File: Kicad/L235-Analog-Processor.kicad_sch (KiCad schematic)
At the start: 224 parts, among them IC1 CA3046Z, J1 Input A, J10 Half Wave In B, J11 Inverted Out B, J12 Invert IN B, J13 Invert IN A, J14 Half Wave In A, J15 Inverted Out A, J16 Full-Wave Rectifier A, J17 Half-Wave Rectifier A, J18 √(A²+B²), J19 A * B / 10, J2 Input B, J20 Root Input |A|, J21 Root Input |A|, J3 Function IN, J4 10A / |B|, J5 Output F(x), J6 Power, J7 Full-Wave Rectifier B, J8 A - B, J9 Half-Wave Rectifier B, Q1 NPN, SW1 71BF30-02-2-06N-circular, SW2 INVERT SWITCH, SW3 71BF30-02-2-06N-circular, SW4 FULL/HALF WAVE, SW6 ADD/SUBTRACT, SW7 POS/NEG HALF WAVE, SW8 INVERT SWITCH, U1 TL082, U10 TL082, U11 TL082, U12 TL082, U13 TL084, U14 CA3046Z, U15 TL082, U16 AD534JH, U16 TL082, U2 TL082, U3 TL082, U4 TL082, U5 TL082, U6 TL082, U7 TL082, U8 TL082, U9 TL082

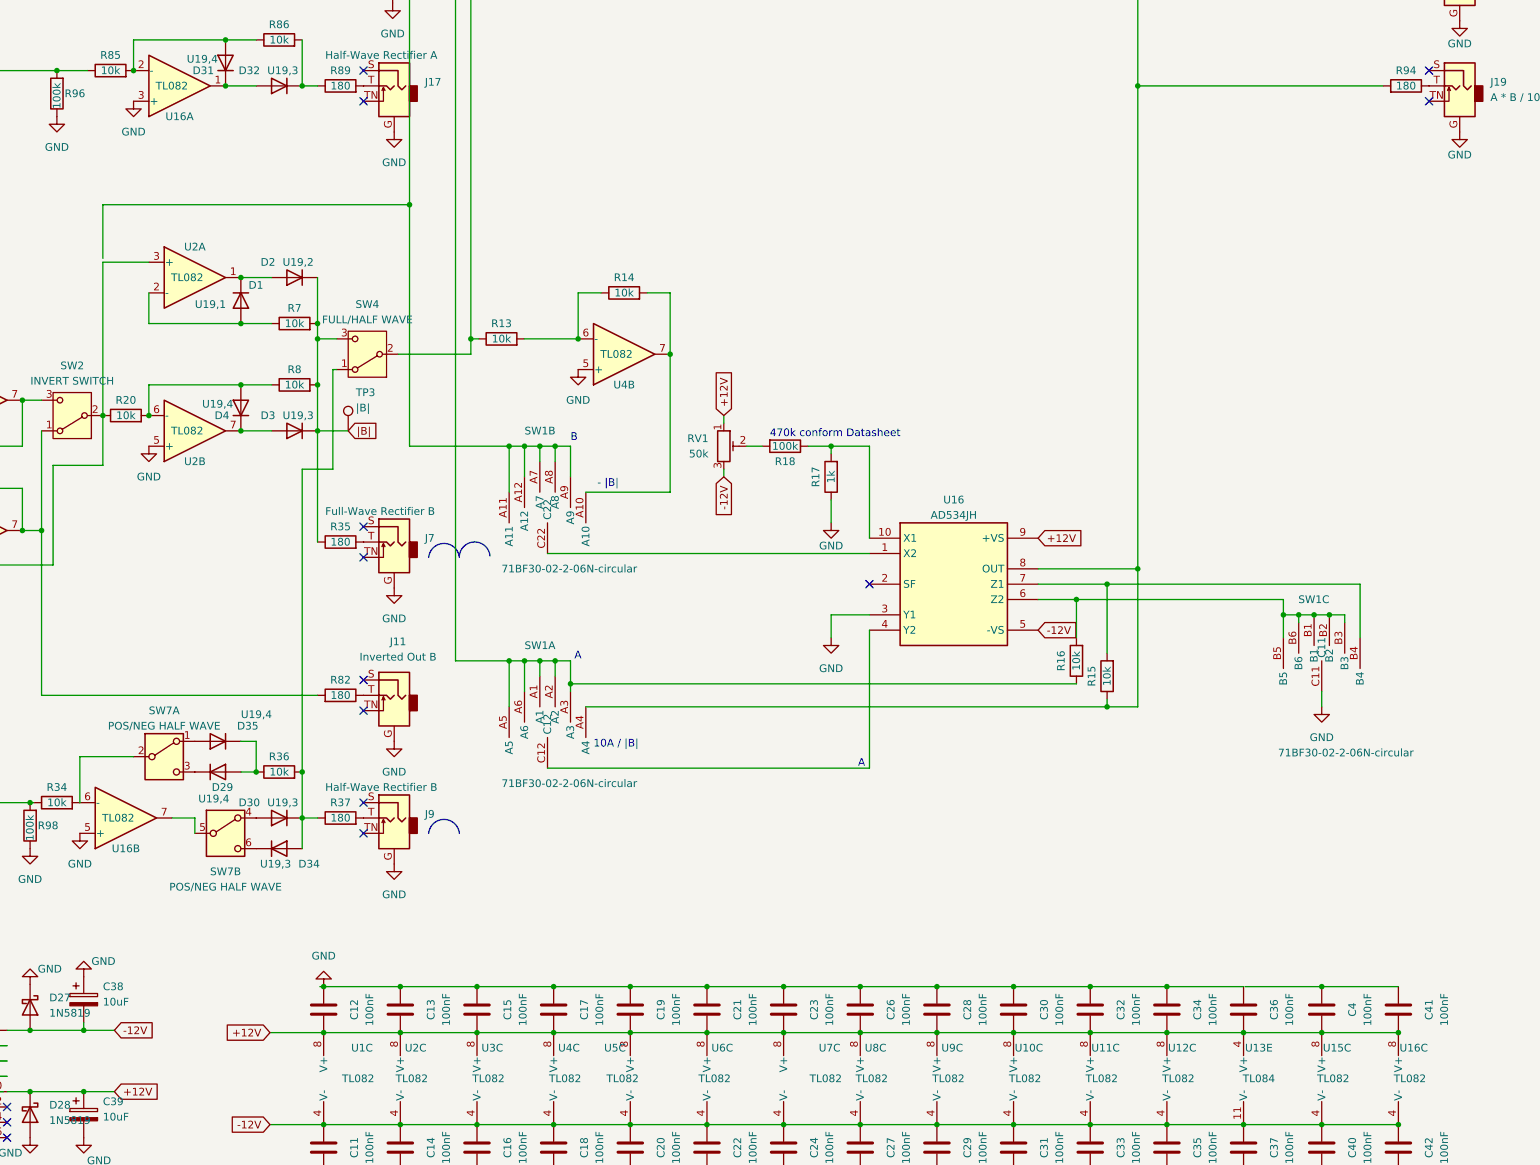
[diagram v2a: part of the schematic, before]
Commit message: fixed double U16 annotation
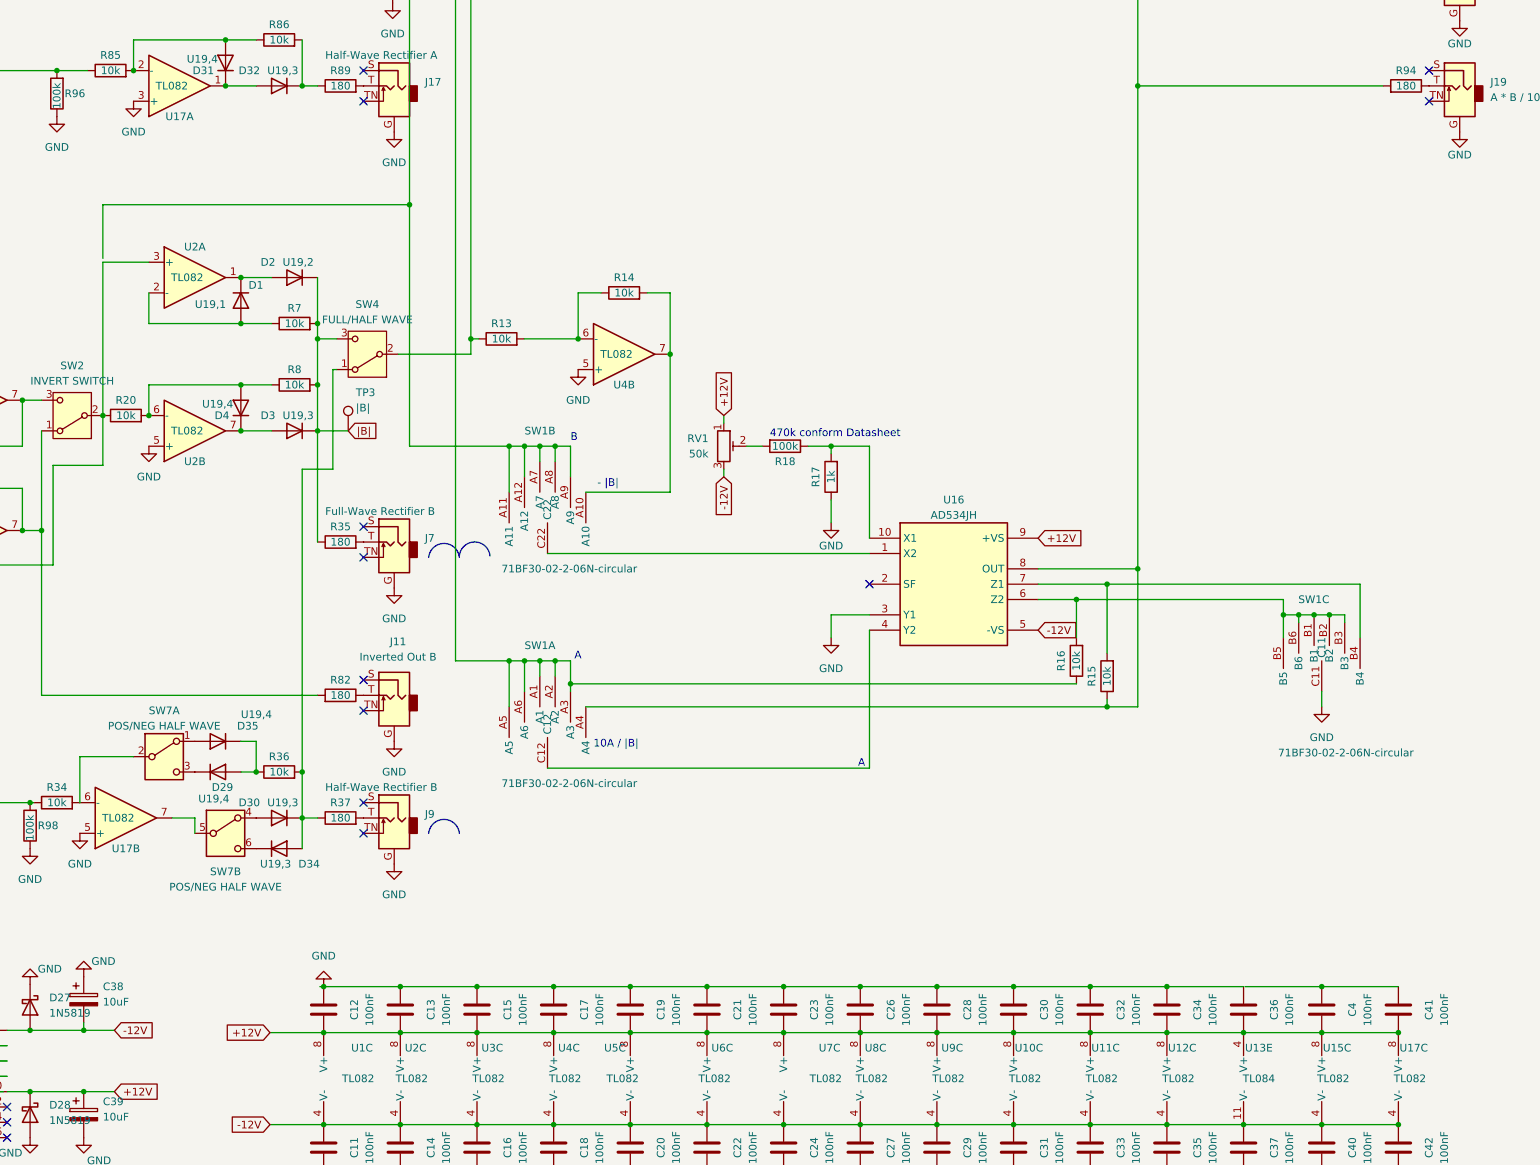
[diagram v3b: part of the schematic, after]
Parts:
- renumbered U16 to U17
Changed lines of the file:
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@@
   (symbol (lib_id "Amplifier_Operational:TL082") (at 287.02 365.76 0) (unit 3)
     (in_bom yes) (on_board yes) (dnp no)
-    (property "Reference" "U16" (at 287.02 360.68 0)
+    (property "Reference" "U17" (at 287.02 360.68 0)
       (effects (font (size 1.27 1.27)))
     )
@@
       (project "L235-Analog-Processor"
         (path "/11565f7a-671a-4a91-8d3b-c6d6401f938b"
-          (reference "U16") (unit 3)
+          (reference "U17") (unit 3)
         )
       )
@@
   (symbol (lib_id "Amplifier_Operational:TL082") (at 73.66 322.58 0) (mirror x) (unit 2)
     (in_bom yes) (on_board yes) (dnp no)
-    (property "Reference" "U16" (at 73.66 327.66 0)
+    (property "Reference" "U17" (at 73.66 327.66 0)
       (effects (font (size 1.27 1.27)))
     )
@@
       (project "L235-Analog-Processor"
         (path "/11565f7a-671a-4a91-8d3b-c6d6401f938b"
-          (reference "U16") (unit 2)
+          (reference "U17") (unit 2)
         )
       )
@@
   (symbol (lib_id "Amplifier_Operational:TL082") (at 82.55 201.295 0) (mirror x) (unit 1)
     (in_bom yes) (on_board yes) (dnp no)
-    (property "Reference" "U16" (at 82.55 206.375 0)
+    (property "Reference" "U17" (at 82.55 206.375 0)
       (effects (font (size 1.27 1.27)))
     )
@@
       (project "L235-Analog-Processor"
         (path "/11565f7a-671a-4a91-8d3b-c6d6401f938b"
-          (reference "U16") (unit 1)
+          (reference "U17") (unit 1)
         )
       )

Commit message: Changed parts to smd and added CV selector
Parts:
- removed D34: U19,3, Diode_THT:D_DO-34_SOD68_P7.62mm_Horizontal, symbol Device:D
- removed D35: U19,4, Diode_THT:D_DO-34_SOD68_P7.62mm_Horizontal, symbol Device:D
- removed IC1, U14: CA3046Z, Package_DIP:DIP-14_W7.62mm_Socket, symbol CA3046Z:CA3046Z
- removed J14: Half Wave In A, Connector_Audio:Jack_3.5mm_PJ311_Horizontal, symbol Connector_Audio:AudioJack2_Ground_SwitchT
- removed J19: A * B / 10, Connector_Audio:Jack_3.5mm_PJ311_Horizontal, symbol Connector_Audio:AudioJack2_Ground_SwitchT
- removed J20, J21: Root Input |A|, Connector_Audio:Jack_3.5mm_PJ311_Horizontal, symbol Connector_Audio:AudioJack2_Ground_SwitchT
- removed Q1: NPN, Resistor_THT:R_Axial_DIN0614_L14.3mm_D5.7mm_P15.24mm_Horizontal, symbol Simulation_SPICE:NPN
- removed R55: 100k, Resistor_THT:R_Axial_DIN0614_L14.3mm_D5.7mm_P15.24mm_Horizontal, symbol Device:R
- removed R56: 1k, Resistor_THT:R_Axial_DIN0614_L14.3mm_D5.7mm_P15.24mm_Horizontal, symbol Device:R
- removed SW1, SW3: 71BF30-02-2-06N-circular, 71BF30-02-2-06N:71BF3002206N, symbol 71BF30-02-2-06N:71BF30-02-2-06N-circular
- removed SW2, SW8: INVERT SWITCH, symbol Switch:SW_SPDT
- removed SW4: FULL/HALF WAVE, symbol Switch:SW_SPDT
- removed SW6: ADD/SUBTRACT, symbol Switch:SW_DPDT_x2
- removed SW7: POS/NEG HALF WAVE, symbol Switch:SW_DPDT_x2
- removed TP3: |B|, TestPoint:TestPoint_THTPad_2.0x2.0mm_Drill1.0mm, symbol Connector:TestPoint
- removed U16: AD534JH, Package_TO_SOT_THT:TO-100-10, symbol AD534LDZ:AD534LDZ
- added C43, C44, C45, C46, C47, C48, C49, C50, C51, C52, C53, C54, C55, C56, C57, C58, C59, C60, C62, C63, C64, C65, C66, C67, C68, C69, C70, C71, C72, C73, C74, C75, C76, C77, C78, C79, C80, C81, C82: 100nF, Capacitor_SMD:C_0402_1005Metric, symbol Device:C
- added C61: 330nF, Capacitor_SMD:C_0402_1005Metric, symbol Device:C
- added IC2: AD633ARZ-RL, Package_SO:SOIC-8_3.9x4.9mm_P1.27mm, symbol AD633ARZ-RL:AD633ARZ-RL
- added R101: 18k, Resistor_SMD:R_0402_1005Metric, symbol Device:R
- added R102, R103, R111, R66: 10k, Resistor_SMD:R_0402_1005Metric, symbol Device:R
- added R104: 4.7k, Resistor_SMD:R_0402_1005Metric, symbol Device:R
- added R105, R106, R107, R108, R109, R113, R60, R61, R62, R90: 1k, Resistor_SMD:R_0402_1005Metric, symbol Device:R
- added R110, R65: 2k, Resistor_SMD:R_0402_1005Metric, symbol Device:R
- added R112: 100k, Resistor_SMD:R_0402_1005Metric, symbol Device:R
- added R63: 4.3k, Resistor_SMD:R_0402_1005Metric, symbol Device:R
- added R64: 3k, Resistor_SMD:R_0402_1005Metric, symbol Device:R
- added RV10, RV9: 100k, Potentiometer_THT:Potentiometer_Alpha_RD901F-40-00D_Single_Vertical, symbol Device:R_Potentiometer
- added RV11, RV12: 50k, Potentiometer_THT:Potentiometer_Alpha_RD901F-40-00D_Single_Vertical, symbol Device:R_Potentiometer
- added TR1, TR2, TR3, TR4, TR5: FMBM5551, Package_TO_SOT_SMD:SOT-23-6_Handsoldering, symbol Macbeth:BC847CDW1T1G
- added U16: RC4580, Package_SO:SOIC-8_3.9x4.9mm_P1.27mm, symbol Amplifier_Operational:RC4580
- added U18: LM4040DBZ-10, Package_TO_SOT_SMD:SOT-23, symbol Reference_Voltage:LM4040DBZ-10
- added U19, U31: 74HC148, Package_SO:SOIC-16W_5.3x10.2mm_P1.27mm, symbol 74xx:74LS348
- added U20, U21, U29, U30: LM339, Package_SO:SOIC-14_3.9x8.7mm_P1.27mm, symbol Comparator:LM339
- added U22, U23, U24, U25, U26, U27, U28, U32, U33, U34, U35: 74LS151, Package_SO:TSSOP-16-1EP_4.4x5mm_P0.65mm_EP3x3mm, symbol 4xxx:4051
- added U36: LM78M05_TO252, Package_TO_SOT_SMD:TO-252-2, symbol Regulator_Linear:LM78M05_TO252
- C1, C11, C12, C13, C14, C15, C16, C17, C18, C19, C2, C20, C21, C22, C23, C24, C26, C27, C28, C29, C30, C31, C32, C33, C34, C35, C36, C37, C4, C40, C41, C42, C5, C6, C8: footprint Capacitor_THT:C_Rect_L7.0mm_W3.5mm_P2.50mm_P5.00mm -> Capacitor_SMD:C_0402_1005Metric
- C10, C25, C3, C7, C9: footprint Capacitor_THT:C_Rect_L7.0mm_W3.5mm_P2.50mm_P5.00mm -> Capacitor_THT:C_Rect_L7.0mm_W2.5mm_P5.00mm
- C38, C39: footprint Capacitor_THT:C_Disc_D5.0mm_W2.5mm_P5.00mm -> Capacitor_THT:C_Radial_D5.0mm_H7.0mm_P2.00mm
- D1, D10, D11, D12, D13, D14, D15, D16, D17, D18, D19, D2, D20, D21, D22, D23, D24, D25, D26, D29, D3, D30, D31, D32, D4, D5, D6, D7, D8, D9: footprint Diode_THT:D_DO-34_SOD68_P7.62mm_Horizontal -> Diode_SMD:D_0402_1005Metric
- D27, D28: footprint Diode_THT:D_DO-41_SOD81_P10.16mm_Horizontal -> Diode_SMD:D_0402_1005Metric
- J1, J11, J15, J16, J17, J18, J2, J3, J5, J7, J8: footprint Connector_Audio:Jack_3.5mm_PJ311_Horizontal -> Custom_Footprints:Cliff_3.5mm_Stereo_Jack
- J10: value Half Wave In B -> Half Wave A + -B; footprint Connector_Audio:Jack_3.5mm_PJ311_Horizontal -> Custom_Footprints:Cliff_3.5mm_Stereo_Jack
- J12: value Invert IN B -> CV Select; footprint Connector_Audio:Jack_3.5mm_PJ311_Horizontal -> Custom_Footprints:Cliff_3.5mm_Stereo_Jack
- J13: value Invert IN A -> CV Select; footprint Connector_Audio:Jack_3.5mm_PJ311_Horizontal -> Custom_Footprints:Cliff_3.5mm_Stereo_Jack
- J4: value 10A / |B| -> ( 10A / |B| ) / ( A * B / 10 ); footprint Connector_Audio:Jack_3.5mm_PJ311_Horizontal -> Custom_Footprints:Cliff_3.5mm_Stereo_Jack
- J6: footprint Resistor_THT:R_Axial_DIN0614_L14.3mm_D5.7mm_P15.24mm_Horizontal -> Custom_Footprints:Eurorack_16_pin_header
- J9: value Half-Wave Rectifier B -> Negative Half-Wave Rectifier B; footprint Connector_Audio:Jack_3.5mm_PJ311_Horizontal -> Custom_Footprints:Cliff_3.5mm_Stereo_Jack
- R1, R10, R11, R12, R13, R14, R17, R19, R20, R21, R22, R23, R24, R25, R26, R27, R28, R29, R3, R30, R31, R32, R33, R34, R35, R36, R37, R39, R40, R41, R42, R43, R44, R45, R46, R47, R48, R49, R5, R50, R51, R52, R53, R54, R57, R58, R59, R6, R67, R68, R69, R7, R70, R71, R72, R73, R74, R75, R76, R77, R78, R79, R8, R80, R81, R82, R84, R85, R86, R87, R88, R89, R9, R91, R92, R93, R99: footprint Resistor_THT:R_Axial_DIN0614_L14.3mm_D5.7mm_P15.24mm_Horizontal -> Resistor_SMD:R_0402_1005Metric
- R100, R4: value 100k -> 10k; footprint Resistor_THT:R_Axial_DIN0614_L14.3mm_D5.7mm_P15.24mm_Horizontal -> Resistor_SMD:R_0402_1005Metric
- R15: value 10k -> 100k; footprint Resistor_THT:R_Axial_DIN0614_L14.3mm_D5.7mm_P15.24mm_Horizontal -> Resistor_SMD:R_0402_1005Metric
- R16: value 10k -> 3k; footprint Resistor_THT:R_Axial_DIN0614_L14.3mm_D5.7mm_P15.24mm_Horizontal -> Resistor_SMD:R_0402_1005Metric
- R18: value 100k -> 300k; footprint Resistor_THT:R_Axial_DIN0614_L14.3mm_D5.7mm_P15.24mm_Horizontal -> Resistor_SMD:R_0402_1005Metric
- R2, R95, R96, R97: value 100k -> 1k; footprint Resistor_THT:R_Axial_DIN0614_L14.3mm_D5.7mm_P15.24mm_Horizontal -> Resistor_SMD:R_0402_1005Metric
- R38: value 10k -> 180; footprint Resistor_THT:R_Axial_DIN0614_L14.3mm_D5.7mm_P15.24mm_Horizontal -> Resistor_SMD:R_0402_1005Metric
- R83: value 10k -> 1k; footprint Resistor_THT:R_Axial_DIN0614_L14.3mm_D5.7mm_P15.24mm_Horizontal -> Resistor_SMD:R_0402_1005Metric
- R94: value 180 -> 1k; footprint Resistor_THT:R_Axial_DIN0614_L14.3mm_D5.7mm_P15.24mm_Horizontal -> Resistor_SMD:R_0402_1005Metric
- R98: value 100k -> 3k; footprint Resistor_THT:R_Axial_DIN0614_L14.3mm_D5.7mm_P15.24mm_Horizontal -> Resistor_SMD:R_0402_1005Metric
- RV1, RV2, RV3, RV4, RV5, RV6: footprint Resistor_THT:R_Axial_DIN0614_L14.3mm_D5.7mm_P15.24mm_Horizontal -> Potentiometer_THT:Potentiometer_Bourns_3339H_Vertical
- RV7: footprint (none) -> Potentiometer_THT:Potentiometer_Alps_RK163_Single_Horizontal
- RV8: footprint Resistor_THT:R_Axial_DIN0614_L14.3mm_D5.7mm_P15.24mm_Horizontal -> Potentiometer_THT:Potentiometer_Alps_RK163_Single_Horizontal
- U1, U10, U11, U12, U2, U3, U4, U5, U6, U7, U8, U9: footprint Package_DIP:DIP-8_W7.62mm_Socket -> Package_SO:SOIC-8_3.9x4.9mm_P1.27mm
- U13: footprint Package_DIP:DIP-14_W7.62mm_Socket -> Package_SO:SOIC-14_3.9x8.7mm_P1.27mm
- U15, U17: footprint Package_DIP:DIP-8_W7.62mm_Socket -> Package_SO:SO-8_3.9x4.9mm_P1.27mm
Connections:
- net +12V: now also C4.1, C41.1, U15.8 (V+), U17.8 (V+), C45.1, C47.1, C49.2, C52.2, C60.2, C61.1, C64.2, C66.2, C67.2, C68.2, C69.2, C70.2, C71.2, C73.2, C82.2, IC2.6 (+VS), U20.3 (V+), U21.3 (V+), U22.16 (VDD), U23.16 (VDD), U24.16 (VDD), U25.16 (VDD), U26.16 (VDD), U27.16 (VDD), U28.16 (VDD), U32.16 (VDD), U33.16 (VDD), U34.16 (VDD), U35.16 (VDD), U36.1 (VI); no longer C11.1, C11.2, C12.2, C13.2, C14.1, C14.2, C15.2, C16.1, C16.2, C17.2, C18.1, C18.2, C19.2, C20.1, C20.2, C21.2, C22.1, C22.2, C23.2, C24.1, C24.2, C26.2, C27.1, C27.2, C28.2, C29.1, C29.2, C3.2, C30.2, C31.1, C31.2, C32.2, C33.1, C33.2, C34.2, C35.1, C35.2, C36.2, C37.1, C37.2, C38.1, C38.2, C39.2, C9.2, D10.1 (K), D26.1 (K), D27.1 (K), D27.2 (A), D28.2 (A), D9.1 (K), J1.G, J10.G, J11.G, J12.G, J13.G, J15.G, J16.G, J17.G, J18.G, J2.G, J3.G, J4.G, J5.G, J6.1 (Pin_1), J6.2 (Pin_2), J6.3 (Pin_3), J6.4 (Pin_4), J6.5 (Pin_5), J6.6 (Pin_6), J6.7 (Pin_7), J6.8 (Pin_8), J7.G, J8.G, J9.G, R10.1, R100.1, R17.1, R25.2, R26.1, R31.1, R4.1, R48.2, R59.1, R71.2, R72.1, R75.1, R76.2, R78.2, R79.2, R80.1, R95.1, R96.1, R97.1, R98.1, R99.1, RV1.3, U1.4 (V-), U10.4 (V-), U10.5 (+), U11.3 (+), U11.4 (V-), U11.5 (+), U12.3 (+), U12.4 (V-), U12.5 (+), U13.10 (+), U13.11 (V-), U13.13 (-), U15.3 (+), U15.5 (+), U17.3 (+), U17.5 (+), U2.4 (V-), U2.5 (+), U3.4 (V-), U3.5 (+), U4.4 (V-), U4.5 (+), U5.3 (+), U5.4 (V-), U6.2 (-), U6.4 (V-), U7.3 (+), U7.4 (V-), U8.4 (V-), U8.5 (+), U9.3 (+), U9.4 (V-)
- net <X>: now also R112.1, R113.1, U34.15 (X2)
- net X: now also U22.3 (X)
- net |A|: now also D5.1 (K), D8.1 (K), R21.1, R5.2, R6.2, R88.1
- net |B|: now also R13.1, RV3.2, RV3.3
- net √|x| or X²: now reaches R54.1, U10.7
- net √|x| or X²: now also U34.12 (X3), U34.14 (X1)
- net (-dX/dt) or (-dX/dt*1/100): now reaches R57.1, R58.2, U7.1
- net (-dX/dt) or (-dX/dt*1/100): now also U34.1 (X4), U34.5 (X5)
- net ln |x|: now reaches RV5.2, RV5.3, U11.7
- net ln |x|: now also U34.13 (X0)
- net Function Out: now reaches D12.2 (A), D17.1 (K), RV8.1
- net Function Out: now also U34.3 (X)
- net at C5.1, R43.2, U9.2 (-): now also TR3.6
- net at C1.1, RV2.3, U5.2 (-): now also TR5.6
- net at R99.2: now also R98.1, R62.2, U20.5 (+); no longer R21.1
- net B: now reaches R20.1, U2.3 (+)
- net B: now also R100.1, R11.1, R34.1, R4.1, U1.6 (-), U1.7, U23.1 (X4), U23.12 (X3), U23.13 (X0), U23.14 (X1), U23.15 (X2); no longer J10.TN
- net at R94.1: now also R95.2, U21.5 (+)
- net at C2.2, R33.1, R33.2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: now also TR2.4
- net GND: now reaches C4.2, C41.2
- net GND: now also C11.1, C12.2, C13.2, C14.1, C15.2, C16.1, C17.2, C18.1, C19.2, C20.1, C21.2, C22.1, C23.2, C24.1, C26.2, C27.1, C28.2, C29.1, C3.2, C30.2, C31.1, C32.2, C33.1, C34.2, C35.1, C36.2, C37.1, C38.1, C39.2, C40.1, C42.1, C9.2, D10.1 (K), D26.1 (K), D27.1 (K), D28.2 (A), D9.1 (K), J1.G, J10.G, J11.G, J12.G, J13.G, J15.G, J16.G, J17.G, J18.G, J2.G, J3.G, J4.G, J5.G, J6.3 (Pin_3), J6.4 (Pin_4), J6.5 (Pin_5), J6.6 (Pin_6), J6.7 (Pin_7), J6.8 (Pin_8), J7.G, J8.G, J9.G, R10.1, R15.1, R17.1, R25.2, R31.1, R48.2, R59.1, R72.1, R75.1, R78.2, R79.2, R80.1, R97.1, R99.1, U10.5 (+), U11.3 (+), U11.5 (+), U12.3 (+), U12.5 (+), U13.10 (+), U13.13 (-), U15.3 (+), U15.5 (+), U17.3 (+), U17.5 (+), U2.5 (+), U3.5 (+), U4.5 (+), U5.3 (+), U6.2 (-), U7.3 (+), U8.5 (+), U9.3 (+), C43.1, C44.1, C45.2, C46.1, C47.2, C48.1, C49.1, C50.1, C51.1, C52.1, C53.1, C54.1, C55.1, C56.1, C57.1, C58.1, C59.1, C60.1, C61.2, C62.1, C63.1, C64.1, C65.1, C66.1, C67.1, C68.1, C69.1, C70.1, C71.1, C72.1, C73.1, C74.2, C75.1, C76.2, C77.1, C78.1, C80.2, C81.1, C82.1, R101.2, R109.1, R111.1, R64.1, R66.1, RV10.3, RV11.3, RV12.3, RV9.3, TR2.3, TR3.1, TR4.3, TR5.1, U16.5 (+), U18.2 (A), U19.5 (EI), U19.8 (GND), U22.6 (Inh), U22.7 (VEE), U23.6 (Inh), U23.7 (VEE), U24.2 (X6), U24.6 (Inh), U24.7 (VEE), U25.6 (Inh), U25.7 (VEE), U26.5 (X5), U26.6 (Inh), U26.7 (VEE), U27.1 (X4), U27.12 (X3), U27.13 (X0), U27.14 (X1), U27.15 (X2), U27.6 (Inh), U27.7 (VEE), U28.1 (X4), U28.12 (X3), U28.13 (X0), U28.14 (X1), U28.15 (X2), U28.5 (X5), U28.6 (Inh), U28.7 (VEE), U31.5 (EI), U31.8 (GND), U32.6 (Inh), U32.7 (VEE), U33.6 (Inh), U33.7 (VEE), U34.6 (Inh), U34.7 (VEE), U35.6 (Inh), U35.7 (VEE), U36.2 (GND)
- net A: now reaches R19.1, R9.1, U3.3 (+)
- net A: now also R84.1, R85.1, U1.1, U1.2 (-), U15.2 (-), R103.1, U24.1 (X4), U24.12 (X3), U24.13 (X0), U24.14 (X1), U24.15 (X2), U27.2 (X6), U28.2 (X6); no longer R16.1
- net 10V REF: now reaches R16.2
- net 10V REF: now also J1.TN, J2.TN, R2.2, R98.2, C43.2, R110.2, R65.2, U18.1 (K)
- net -12V: now reaches C40.2, C42.2, U15.4 (V-), U17.4 (V-)
- net -12V: now also C11.2, C14.2, C16.2, C18.2, C20.2, C22.2, C24.2, C27.2, C29.2, C31.2, C33.2, C35.2, C37.2, C38.2, D27.2 (A), J6.1 (Pin_1), J6.2 (Pin_2), R26.1, R71.2, R76.2, RV1.3, U1.4 (V-), U10.4 (V-), U11.4 (V-), U12.4 (V-), U13.11 (V-), U2.4 (V-), U3.4 (V-), U4.4 (V-), U5.4 (V-), U6.4 (V-), U7.4 (V-), U8.4 (V-), U9.4 (V-), C44.2, C46.2, C50.2, C51.2, C53.2, C54.2, C55.2, C57.2, C58.2, C59.2, C63.2, C65.2, C72.2, C75.2, C77.2, C78.2, C81.2, IC2.3 (-VS), U16.4 (V-), U20.12 (V-), U21.12 (V-), U22.8 (VSS), U23.8 (VSS), U24.8 (VSS), U25.8 (VSS), U26.8 (VSS), U27.8 (VSS), U28.8 (VSS), U29.12 (V-), U30.12 (V-), U32.8 (VSS), U33.8 (VSS), U34.8 (VSS), U35.8 (VSS)
- net at R96.2: now also R95.1, U21.11 (+); no longer R85.1
- net at R45.1, U9.5 (+): now also TR3.3, TR3.4
- net X²: now reaches D26.2 (A), R46.1, R49.2, U9.7
- net X²: now also U35.1 (X4), U35.12 (X3), U35.5 (X5)
- net B|: now reaches D30.1 (K), R36.2, R37.1
- net B|: now also D32.1 (K), R38.1, R86.2, R89.1
- net at D30.2 (A): now also D29.1 (K), U17.7
- net at R36.1: now also D29.2 (A), R34.2, U17.6 (-); no longer D29.1 (K)
- net at R9.2, U4.3 (+): now also R10.2
- net at R12.1, U4.2 (-): now also R11.2
- net √|x|: now reaches R47.2, R48.1
- net √|x|: now also U35.13 (X0), U35.14 (X1), U35.15 (X2)
- net CA3046_B3: now reaches U10.3 (+)
- net CA3046_B3: now also TR4.1, U35.3 (X)
- net F1: now reaches C7.2, R57.2, U7.2 (-)
- net F1: now also U33.12 (X3), U33.13 (X0), U33.14 (X1), U33.15 (X2), U33.5 (X5)
- net -A: now reaches R84.2, R87.2, U15.1
- net F2: now reaches R58.1
- net F2: now also U33.3 (X)
- net -Output: now reaches D13.2 (A), D16.1 (K), R67.1, R68.2, U12.7
- net at R30.1, U13.1, U13.2 (-): now also TR2.5
- net at R22.2, R23.1: now also TR5.5
- net at R29.2, R32.2: now also TR2.2
- net at R44.2: now also TR3.2, TR3.5
- net at C25.1, R27.1, U11.2 (-): now also TR1.4, TR1.6
- net at R24.2, U5.7: now also TR1.1
- net at R28.1, U6.7: now also TR1.3
- net Volt_ref_X: now reaches R17.2, R18.1
- net Volt_ref_X: now also U25.1 (X4), U25.12 (X3), U25.13 (X0), U25.14 (X1), U25.15 (X2), U25.5 (X5)
- net at R15.2: now also R16.1, R60.2, U29.5 (+)
- net at R39.1, U15.6 (-): now also R4.2; no longer R38.2
- net -B: now reaches R39.2, R82.2, U15.7
- net at R54.2, U10.6 (-): now also TR4.4
- net -|B|: now reaches R14.2, U4.7
- net -|B|: now also U23.5 (X5)
- net F1-1/100: now reaches C7.1
- net F1-1/100: now also U32.3 (X)
- net √(A²+B²): now reaches C25.2, R27.2, R93.2, U11.1
- net √(A²+B²): now also U22.14 (X1)
- net at C6.1, R52.1, U10.2 (-): now also TR4.6
- net at R53.2: now also TR4.2, TR4.5
- net A - B: now reaches R12.2, R92.2, U4.1
- net A - B: now also U22.1 (X4)
- new net: C74.1, C76.1, C80.1, U16.8 (V+), U29.3 (V+), U30.3 (V+)
- new net: J13.T, R110.1, R111.2, RV12.1
- new net: R112.2, U32.1 (X4)
- new net: J12.T, R65.1, R66.2, RV11.1
- new net: U29.1, U31.12 (2)
- new net: R60.1, R61.2, U29.7 (+)
- new net: R90.1, R94.2, U20.9 (+)
- new net: J10.T, R38.2
- new net: R102.2, U26.1 (X4), U26.12 (X3), U26.13 (X0), U26.14 (X1), U26.15 (X2)
- new net: R108.1, R109.2, U30.9 (+)
- new net: R107.1, R108.2, U30.11 (+)
- new net: U19.2 (5), U21.2
- new net: IC2.4 (Z), U16.1
- new net: R103.2, U27.5 (X5)
- new net: TR1.2, TR1.5, TR2.1, TR2.6
- new net: U30.14, U31.4 (7)
- new net: R105.2, R61.1, U29.11 (+)
- new net: U29.13, U31.13 (3)
- new net: U29.14, U31.1 (4)
- new net: R105.1, R106.2, U29.9 (+)
- new net: U29.2, U31.11 (1)
- new net: R83.1, R90.2, U20.11 (+)
- new net: U19.11 (1), U20.2
- new net: J2.T, RV10.1
- new net: R62.1, R83.2, U20.7 (+)
- new net: J1.T, RV9.1
- new net: R1.1, RV9.2
- new net: U19.13 (3), U20.13
- new net: U30.2, U31.2 (5)
- new net: U30.13, U31.3 (6)
- new net: R100.2, R101.1, U23.2 (X6)
- new net: U19.1 (4), U20.14
- new net: R104.2, U26.2 (X6)
- new net: U19.4 (7), U21.14
- new net: R96.1, R97.2, U21.9 (+)
- new net: R113.2, U32.5 (X5)
- new net: R106.1, R107.2, U30.5 (+)
- new net: U16.6 (-), U16.7
- new net: R3.1, RV10.2
- new net: U19.12 (2), U20.1
- new net: U19.3 (6), U21.13
- new net * OUT: R91.2
- new net +5V: C48.2, C56.2, C62.2, U19.15 (E0), U19.16 (VCC), U31.15 (E0), U31.16 (VCC), U36.3 (VO)
- new net A0: U19.9 (A0), U22.11 (A), U23.11 (A), U24.11 (A), U25.11 (A), U26.11 (A), U27.11 (A), U28.11 (A)
- new net A1: U19.7 (A1), U22.10 (B), U23.10 (B), U24.10 (B), U25.10 (B), U26.10 (B), U27.10 (B), U28.10 (B)
- new net A2: U19.6 (A2), U22.9 (C), U23.9 (C), U24.9 (C), U25.9 (C), U26.9 (C), U27.9 (C), U28.9 (C)
- new net AD534_OUT: IC2.5 (W), R102.1, R104.1, R63.2, U22.13 (X0), U22.2 (X6), U22.5 (X5), U24.5 (X5)
- new net AD534_X1: IC2.7 (X1), U25.3 (X)
- new net AD534_X2: IC2.8 (X2), U23.3 (X)
- new net AD534_Y1: IC2.1 (Y1), U28.3 (X)
- new net AD534_Y2: IC2.2 (Y2), U24.3 (X)
- new net AD534_Z1: U16.3 (+), U26.3 (X)
- new net AD534_Z2: U16.2 (-), U27.3 (X)
- new net A_IN_BUFFERED: U22.15 (X2)
- new net B0: U31.9 (A0), U32.11 (A), U33.11 (A), U34.11 (A), U35.11 (A)
- new net B1: U31.7 (A1), U32.10 (B), U33.10 (B), U34.10 (B), U35.10 (B)
- new net B2: U31.6 (A2), U32.9 (C), U33.9 (C), U34.9 (C), U35.9 (C)
- new net B_IN_BUFFERED: U22.12 (X3)
- new net CV_FUNCTION: RV12.2, U29.10 (-), U29.4 (-), U29.6 (-), U29.8 (-), U30.10 (-), U30.4 (-), U30.8 (-)
- new net CV_SELECT: RV11.2, U20.10 (-), U20.4 (-), U20.6 (-), U20.8 (-), U21.10 (-), U21.4 (-), U21.8 (-)
- new net Sine: R63.1, R64.2, U25.2 (X6)
- now unconnected: J12.TN, J13.TN
- no-connect marks 51 -> 54
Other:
- note added: "470k on original"
- note added: "ARGUMENT FILTER"
- note added: "FUNCTION"
- note added: "OVERLOAD LED"
- note added: "Sine generator"
- note removed: "- |B|"
- note removed: "470k conform Datasheet"
- note removed: "<X>"
- note removed: "A"
- note removed: "A * B / 10"
- note removed: "A - B"
- note removed: "Argument Filter"
- note removed: "B"
- note removed: "X"
- note removed: "X²"
- moved on the sheet: C7, D1, D2, D3, D31, D32, D4, D5, D6, D7, D8, J1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

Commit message: Added header and mounting points
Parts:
- added J14: Conn_01x12_Pin, Connector_PinHeader_2.54mm:PinHeader_1x18_P2.54mm_Vertical, symbol Connector:Conn_01x18_Pin
- added J19: Conn_01x12_Socket, Connector_PinHeader_2.54mm:PinHeader_1x18_P2.54mm_Vertical, symbol Connector:Conn_01x18_Socket
- C10: value 0.01uF -> 10nF; footprint Capacitor_THT:C_Rect_L7.0mm_W2.5mm_P5.00mm -> Capacitor_SMD:C_0402_1005Metric
- C9: value 0.001uF -> 1nF; footprint Capacitor_THT:C_Rect_L7.0mm_W2.5mm_P5.00mm -> Capacitor_SMD:C_0402_1005Metric
- D24: footprint Diode_SMD:D_0402_1005Metric -> LED_THT:LED_D3.0mm_Clear
- J6: footprint Custom_Footprints:Eurorack_16_pin_header -> Custom_Footprints:Eurorack_10_pin_header; symbol Connector_Generic:Conn_02x08_Odd_Even -> Connector_Generic:Conn_02x05_Odd_Even
- RV7, RV8: footprint Potentiometer_THT:Potentiometer_Alps_RK163_Single_Horizontal -> Potentiometer_THT:Potentiometer_Alpha_RD901F-40-00D_Single_Vertical
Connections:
- net * OUT is gone; now on net AD534_OUT: R91.2
- net A_IN_BUFFERED is gone; now on net A: U22.15 (X2)
- net B_IN_BUFFERED is gone; now on net B: U22.12 (X3)
- net +12V: now also J14.7 (Pin_7), J19.7 (Pin_7)
- net -12V: now also J14.9 (Pin_9), J19.9 (Pin_9)
- net 10V REF: now also J14.12 (Pin_12), J19.12 (Pin_12)
- net <X>: now also J14.11 (Pin_11), J19.11 (Pin_11)
- net A: now also J14.2 (Pin_2), J19.2 (Pin_2)
- net A - B: now also J14.14 (Pin_14), J19.14 (Pin_14)
- net AD534_OUT: now also J14.15 (Pin_15), J19.15 (Pin_15)
- net B: now also J14.4 (Pin_4), J19.4 (Pin_4)
- net CV_FUNCTION: now also J14.18 (Pin_18), J19.18 (Pin_18)
- net CV_SELECT: now also J14.1 (Pin_1), J19.1 (Pin_1)
- net Function Out: now also J14.10 (Pin_10), J19.10 (Pin_10)
- net GND: now also J14.13 (Pin_13), J14.17 (Pin_17), J14.8 (Pin_8), J19.13 (Pin_13), J19.17 (Pin_17), J19.8 (Pin_8)
- net X: now also J14.6 (Pin_6), J19.6 (Pin_6)
- net |A|: now also J14.3 (Pin_3), J19.3 (Pin_3)
- net |B|: now also J14.5 (Pin_5), J19.5 (Pin_5)
- net √(A²+B²): now also J14.16 (Pin_16), J19.16 (Pin_16)
- no-connect marks 54 -> 48

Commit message: Optimized PCB routing, started with variable resistor
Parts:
- removed unit 1 of U13
- removed unit 2 of U16
- added H1, H2, H3: MountingHole, MountingHole:MountingHole_3.2mm_M3_DIN965, symbol Mechanical:MountingHole
- added unit 1 of U11
- added unit 2 of U14
- added unit 2 of U37
- C25: footprint Capacitor_THT:C_Rect_L7.0mm_W2.5mm_P5.00mm -> Capacitor_SMD:C_0402_1005Metric
- U22, U23, U24, U25, U26, U28, U32, U33, U34, U35: value 74LS151 -> DG4051E
- renumbered U16 to U14, U11 to U37
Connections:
- net (-dX/dt) or (-dX/dt*1/100): now also U11.1; no longer U7.1
- net -12V: now also J14.8 (Pin_8), J19.8 (Pin_8); no longer J14.9 (Pin_9), J19.9 (Pin_9)
- net A: now also J14.6 (Pin_6), J19.6 (Pin_6); no longer J14.2 (Pin_2), J19.2 (Pin_2)
- net B: now also J14.9 (Pin_9), J19.9 (Pin_9); no longer J14.4 (Pin_4), J19.4 (Pin_4)
- net F1: now also U11.2 (-); no longer U7.2 (-)
- net GND: now also J14.16 (Pin_16), J19.16 (Pin_16), U7.2 (-), U11.3 (+), U14.6 (-); no longer J14.8 (Pin_8), J15.G, J19.8 (Pin_8), U7.3 (+)
- net X: now also J14.2 (Pin_2), J19.2 (Pin_2); no longer J14.6 (Pin_6), J19.6 (Pin_6)
- net √(A²+B²): now also J14.4 (Pin_4), J19.4 (Pin_4); no longer J14.16 (Pin_16), J19.16 (Pin_16)
- net at R33.2, RV3.1, TR2.4: no longer C2.2, R33.1, U6.3 (+)
- net at R25.1, R26.2: now also U37.6 (-)
- net at R30.1, TR2.5: now also U37.5 (+), U37.7
- new net: C2.2, R33.1, U6.3 (+)
- new net: U7.1, U7.3 (+)
- new net: U14.5 (+), U14.7
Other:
- note added: "1 or 1/100"
- note added: "10V REF"
- note added: "5V Regulator"
- note added: "A - B"
- note added: "Buffered input A"
- note added: "Buffered input B"
- note added: "Full Wave Rectifier A"
- note added: "Full Wave Rectifier B"
- note added: "Full Wave Rectifier X"
- note added: "Half Wave Rectifier A"
- note added: "Invert A"
- note added: "Invert B"
- note added: "Invert |B|"
- note added: "Multiplier IC"
- note added: "Negative Half Wave Rectifier"
- note added: "OUTPUT"
- note added: "UNUSED"
- note removed: "OUTPUT GAIN"
- moved on the sheet: C4, C40, C41, C42, C44, C45, C46, C47, C74, C75, C76, C77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

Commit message: All components routed
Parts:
- removed C79: 100nF, Capacitor_SMD:C_0402_1005Metric, symbol Device:C
- removed D27, D28: 1N5819, Diode_SMD:D_0402_1005Metric, symbol Diode:1N5819
- added D33, D34: 1N5819HW, Diode_SMD:D_SOD-123, symbol Device:D
- added unit 1 of U13
- C17, C18: now not fitted
- J14: value Conn_01x12_Pin -> Conn_01x20_Pin; footprint Connector_PinHeader_2.54mm:PinHeader_1x18_P2.54mm_Vertical -> Connector_PinHeader_2.54mm:PinHeader_1x20_P2.54mm_Vertical; symbol Connector:Conn_01x18_Pin -> Connector:Conn_01x20_Pin
- J19: value Conn_01x12_Socket -> Conn_01x20_Socket; footprint Connector_PinHeader_2.54mm:PinHeader_1x18_P2.54mm_Vertical -> Connector_PinHeader_2.54mm:PinHeader_1x20_P2.54mm_Vertical; symbol Connector:Conn_01x18_Socket -> Connector:Conn_01x20_Socket
- renumbered IC2 to U16
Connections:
- net +12V: now also C74.1, C76.1, C80.1, J14.9 (Pin_9), J19.9 (Pin_9), U14.8 (V+), U29.3 (V+), U30.3 (V+), D34.1 (K); no longer J14.7 (Pin_7), J19.7 (Pin_7)
- net -12V: now also J14.10 (Pin_10), J19.10 (Pin_10), D33.2 (A); no longer J14.8 (Pin_8), J19.8 (Pin_8)
- net 10V REF: now also J14.14 (Pin_14), J19.14 (Pin_14); no longer J14.12 (Pin_12), J19.12 (Pin_12)
- net <X>: now also J14.13 (Pin_13), J19.13 (Pin_13); no longer J14.11 (Pin_11), J19.11 (Pin_11)
- net A: now also J14.8 (Pin_8), J19.8 (Pin_8); no longer J14.6 (Pin_6), J19.6 (Pin_6)
- net A - B: now also J14.16 (Pin_16), J19.16 (Pin_16); no longer J14.14 (Pin_14), J19.14 (Pin_14)
- net AD534_OUT: now also J14.17 (Pin_17), J19.17 (Pin_17); no longer J14.15 (Pin_15), J19.15 (Pin_15)
- net B: now also J14.11 (Pin_11), J19.11 (Pin_11); no longer J14.9 (Pin_9), J19.9 (Pin_9)
- net CV_FUNCTION: now also J14.20 (Pin_20), J19.20 (Pin_20); no longer J14.18 (Pin_18), J19.18 (Pin_18)
- net CV_SELECT: now also J14.3 (Pin_3), J19.3 (Pin_3); no longer J14.1 (Pin_1), J19.1 (Pin_1)
- net Function Out: now also J14.12 (Pin_12), J19.12 (Pin_12); no longer J14.10 (Pin_10), J19.10 (Pin_10)
- net GND: now also J14.15 (Pin_15), J14.18 (Pin_18), J14.19 (Pin_19), J14.2 (Pin_2), J19.15 (Pin_15), J19.18 (Pin_18), J19.19 (Pin_19), J19.2 (Pin_2), D33.1 (K), D34.2 (A), U13.2 (-); no longer J14.13 (Pin_13), J14.16 (Pin_16), J14.17 (Pin_17), J19.13 (Pin_13), J19.16 (Pin_16), J19.17 (Pin_17)
- net X: now also J14.4 (Pin_4), J19.4 (Pin_4); no longer J14.2 (Pin_2), J19.2 (Pin_2)
- net |A|: now also J14.5 (Pin_5), J19.5 (Pin_5); no longer J14.3 (Pin_3), J19.3 (Pin_3)
- net |B|: now also J14.7 (Pin_7), J19.7 (Pin_7); no longer J14.5 (Pin_5), J19.5 (Pin_5)
- net √(A²+B²): now also J14.6 (Pin_6), J19.6 (Pin_6); no longer J14.4 (Pin_4), J19.4 (Pin_4)
- new net: U13.1, U13.3 (+)
- no-connect marks 48 -> 50
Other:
- note added: "2X GAIN"
- note added: "5V in"
- note added: "Already capacitor nearby"
- moved on the sheet: C4, C40, C41, C42, C44, C45, C46, C47, C74, C75, C76, C77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
